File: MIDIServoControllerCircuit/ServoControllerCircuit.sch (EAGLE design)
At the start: 26 parts, among them Q1 20MHz, T1 2N3904, X1 SIGNAL-PWR-GND, X2 SIGNAL-PWR-GND

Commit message: Renamed directory to better reflect what files represent
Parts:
- D1: value 1N4198 -> 1N4148
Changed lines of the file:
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@@
 <part name="C1" library="resistor" deviceset="C-EU" device="050-025X075" value="22p"/>
 <part name="C2" library="resistor" deviceset="C-EU" device="050-025X075" value="22p"/>
-<part name="D1" library="diode" deviceset="1N4148" device="DO35-10" value="1N4198"/>
+<part name="D1" library="diode" deviceset="1N4148" device="DO35-10" value="1N4148"/>
 <part name="Q1" library="special" deviceset="XTAL/S" device="" value="20MHz"/>
 <part name="C3" library="resistor" deviceset="C-EU" device="050-025X075" value="0.1u"/>

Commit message: Renamed PWM outputs to better match what they go to
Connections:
- net SERVO1 renamed EYEBROW
- net SERVO2 renamed LEFT_LIP_CORNER
- net SERVO3 renamed RIGHT_LIP_CORNER
- net SERVO4 renamed LOWER_JAR
- net SERVO5 renamed EYELIDS
- net SERVO6 renamed UNUSED
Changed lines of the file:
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@@
 <instance part="GND8" gate="1" x="78.74" y="76.2" rot="R270"/>
 <instance part="GND9" gate="1" x="124.46" y="27.94" rot="R270"/>
-<instance part="GND10" gate="1" x="111.76" y="99.06"/>
-<instance part="GND11" gate="1" x="111.76" y="81.28"/>
-<instance part="GND13" gate="1" x="154.94" y="53.34"/>
-<instance part="GND14" gate="1" x="154.94" y="35.56"/>
+<instance part="GND10" gate="1" x="106.68" y="99.06"/>
+<instance part="GND11" gate="1" x="106.68" y="81.28"/>
+<instance part="GND13" gate="1" x="149.86" y="53.34"/>
+<instance part="GND14" gate="1" x="149.86" y="35.56"/>
 <instance part="MIDI_PIN-4" gate="1" x="25.4" y="81.28" smashed="yes" rot="R180">
 <attribute name="NAME" x="36.703" y="84.5058" size="1.778" layer="95" rot="R180"/>
@@
 <segment>
 <pinref part="PIC16F628A" gate="G$1" pin="7"/>
-<wire x1="55.88" y1="17.78" x2="43.18" y2="17.78" width="0.1524" layer="91"/>
-<wire x1="43.18" y1="17.78" x2="43.18" y2="2.54" width="0.1524" layer="91"/>
-<label x="43.18" y="2.54" size="1.778" layer="95" rot="R180" xref="yes"/>
+<wire x1="55.88" y1="17.78" x2="50.8" y2="17.78" width="0.1524" layer="91"/>
+<wire x1="50.8" y1="17.78" x2="50.8" y2="2.54" width="0.1524" layer="91"/>
+<label x="50.8" y="2.54" size="1.778" layer="95" rot="R180" xref="yes"/>
 </segment>
 </net>
@@
 <segment>
 <pinref part="X2" gate="-3" pin="S"/>
-<wire x1="114.3" y1="104.14" x2="111.76" y2="104.14" width="0.1524" layer="91"/>
-<wire x1="111.76" y1="104.14" x2="111.76" y2="101.6" width="0.1524" layer="91"/>
+<wire x1="114.3" y1="104.14" x2="106.68" y2="104.14" width="0.1524" layer="91"/>
+<wire x1="106.68" y1="104.14" x2="106.68" y2="101.6" width="0.1524" layer="91"/>
 <pinref part="GND10" gate="1" pin="GND"/>
 </segment>
 <segment>
 <pinref part="X2" gate="-6" pin="S"/>
-<wire x1="114.3" y1="86.36" x2="111.76" y2="86.36" width="0.1524" layer="91"/>
-<wire x1="111.76" y1="86.36" x2="111.76" y2="83.82" width="0.1524" layer="91"/>
+<wire x1="114.3" y1="86.36" x2="106.68" y2="86.36" width="0.1524" layer="91"/>
+<wire x1="106.68" y1="86.36" x2="106.68" y2="83.82" width="0.1524" layer="91"/>
 <pinref part="GND11" gate="1" pin="GND"/>
 </segment>
 <segment>
 <pinref part="X1" gate="-3" pin="S"/>
-<wire x1="157.48" y1="58.42" x2="154.94" y2="58.42" width="0.1524" layer="91"/>
-<wire x1="154.94" y1="58.42" x2="154.94" y2="55.88" width="0.1524" layer="91"/>
+<wire x1="157.48" y1="58.42" x2="149.86" y2="58.42" width="0.1524" layer="91"/>
+<wire x1="149.86" y1="58.42" x2="149.86" y2="55.88" width="0.1524" layer="91"/>
 <pinref part="GND13" gate="1" pin="GND"/>
 </segment>
 <segment>
 <pinref part="X1" gate="-6" pin="S"/>
-<wire x1="157.48" y1="40.64" x2="154.94" y2="40.64" width="0.1524" layer="91"/>
-<wire x1="154.94" y1="40.64" x2="154.94" y2="38.1" width="0.1524" layer="91"/>
+<wire x1="157.48" y1="40.64" x2="149.86" y2="40.64" width="0.1524" layer="91"/>
+<wire x1="149.86" y1="40.64" x2="149.86" y2="38.1" width="0.1524" layer="91"/>
 <pinref part="GND14" gate="1" pin="GND"/>
 </segment>
@@
 </segment>
 </net>
-<net name="SERVO3" class="0">
+<net name="RIGHT_LIP_CORNER" class="0">
 <segment>
 <pinref part="PIC16F628A" gate="G$1" pin="1"/>
@@
 <pinref part="X2" gate="-7" pin="S"/>
 <wire x1="114.3" y1="73.66" x2="111.76" y2="73.66" width="0.1524" layer="91"/>
-<wire x1="111.76" y1="73.66" x2="111.76" y2="76.2" width="0.1524" layer="91"/>
-<label x="111.76" y="76.2" size="1.778" layer="95" rot="R180" xref="yes"/>
-</segment>
-</net>
-<net name="SERVO1" class="0">
+<wire x1="111.76" y1="73.66" x2="111.76" y2="78.74" width="0.1524" layer="91"/>
+<label x="111.76" y="78.74" size="1.778" layer="95" xref="yes"/>
+</segment>
+</net>
+<net name="EYEBROW" class="0">
 <segment>
 <pinref part="PIC16F628A" gate="G$1" pin="17"/>
@@
 <pinref part="X2" gate="-1" pin="S"/>
 <wire x1="114.3" y1="109.22" x2="111.76" y2="109.22" width="0.1524" layer="91"/>
-<wire x1="111.76" y1="114.3" x2="111.76" y2="109.22" width="0.1524" layer="91"/>
-<label x="111.76" y="114.3" size="1.778" layer="95" rot="R180" xref="yes"/>
-</segment>
-</net>
-<net name="SERVO2" class="0">
+<wire x1="111.76" y1="116.84" x2="111.76" y2="109.22" width="0.1524" layer="91"/>
+<label x="111.76" y="116.84" size="1.778" layer="95" xref="yes"/>
+</segment>
+</net>
+<net name="LEFT_LIP_CORNER" class="0">
 <segment>
 <pinref part="PIC16F628A" gate="G$1" pin="18"/>
@@
 <pinref part="X2" gate="-4" pin="S"/>
 <wire x1="114.3" y1="91.44" x2="111.76" y2="91.44" width="0.1524" layer="91"/>
-<wire x1="111.76" y1="91.44" x2="111.76" y2="93.98" width="0.1524" layer="91"/>
-<label x="111.76" y="93.98" size="1.778" layer="95" rot="R180" xref="yes"/>
-</segment>
-</net>
-<net name="SERVO4" class="0">
+<wire x1="111.76" y1="91.44" x2="111.76" y2="96.52" width="0.1524" layer="91"/>
+<label x="111.76" y="96.52" size="1.778" layer="95" xref="yes"/>
+</segment>
+</net>
+<net name="LOWER_JAR" class="0">
 <segment>
 <pinref part="PIC16F628A" gate="G$1" pin="2"/>
@@
 <pinref part="X1" gate="-1" pin="S"/>
 <wire x1="157.48" y1="63.5" x2="154.94" y2="63.5" width="0.1524" layer="91"/>
-<wire x1="154.94" y1="63.5" x2="154.94" y2="66.04" width="0.1524" layer="91"/>
-<label x="154.94" y="66.04" size="1.778" layer="95" rot="R180" xref="yes"/>
-</segment>
-</net>
-<net name="SERVO5" class="0">
+<wire x1="154.94" y1="63.5" x2="154.94" y2="71.12" width="0.1524" layer="91"/>
+<label x="154.94" y="71.12" size="1.778" layer="95" xref="yes"/>
+</segment>
+</net>
+<net name="EYELIDS" class="0">
 <segment>
 <pinref part="PIC16F628A" gate="G$1" pin="6"/>
-<wire x1="55.88" y1="20.32" x2="38.1" y2="20.32" width="0.1524" layer="91"/>
-<wire x1="38.1" y1="20.32" x2="38.1" y2="7.62" width="0.1524" layer="91"/>
-<label x="38.1" y="7.62" size="1.778" layer="95" rot="R180" xref="yes"/>
+<wire x1="55.88" y1="20.32" x2="45.72" y2="20.32" width="0.1524" layer="91"/>
+<wire x1="45.72" y1="20.32" x2="45.72" y2="7.62" width="0.1524" layer="91"/>
+<label x="45.72" y="7.62" size="1.778" layer="95" rot="R180" xref="yes"/>
 </segment>
 <segment>
 <pinref part="X1" gate="-4" pin="S"/>
 <wire x1="157.48" y1="45.72" x2="154.94" y2="45.72" width="0.1524" layer="91"/>
-<wire x1="154.94" y1="45.72" x2="154.94" y2="48.26" width="0.1524" layer="91"/>
-<label x="154.94" y="48.26" size="1.778" layer="95" rot="R180" xref="yes"/>
-</segment>
-</net>
-<net name="SERVO6" class="0">
+<wire x1="154.94" y1="45.72" x2="154.94" y2="50.8" width="0.1524" layer="91"/>
+<label x="154.94" y="50.8" size="1.778" layer="95" xref="yes"/>
+</segment>
+</net>
+<net name="UNUSED" class="0">
 <segment>
 <pinref part="PIC16F628A" gate="G$1" pin="9"/>
 <wire x1="55.88" y1="12.7" x2="53.34" y2="12.7" width="0.1524" layer="91"/>
-<wire x1="53.34" y1="12.7" x2="53.34" y2="2.54" width="0.1524" layer="91"/>
-<label x="53.34" y="2.54" size="1.778" layer="95" xref="yes"/>
+<wire x1="53.34" y1="12.7" x2="53.34" y2="0" width="0.1524" layer="91"/>
+<label x="53.34" y="0" size="1.778" layer="95" xref="yes"/>
 </segment>
 <segment>
 <pinref part="X1" gate="-7" pin="S"/>
 <wire x1="157.48" y1="27.94" x2="154.94" y2="27.94" width="0.1524" layer="91"/>
-<wire x1="154.94" y1="27.94" x2="154.94" y2="30.48" width="0.1524" layer="91"/>
-<label x="154.94" y="30.48" size="1.778" layer="95" rot="R180" xref="yes"/>
-</segment>
-</net>
+<wire x1="154.94" y1="27.94" x2="154.94" y2="33.02" width="0.1524" layer="91"/>
+<label x="154.94" y="33.02" size="1.778" layer="95" xref="yes"/>
+</segment>
+</net>

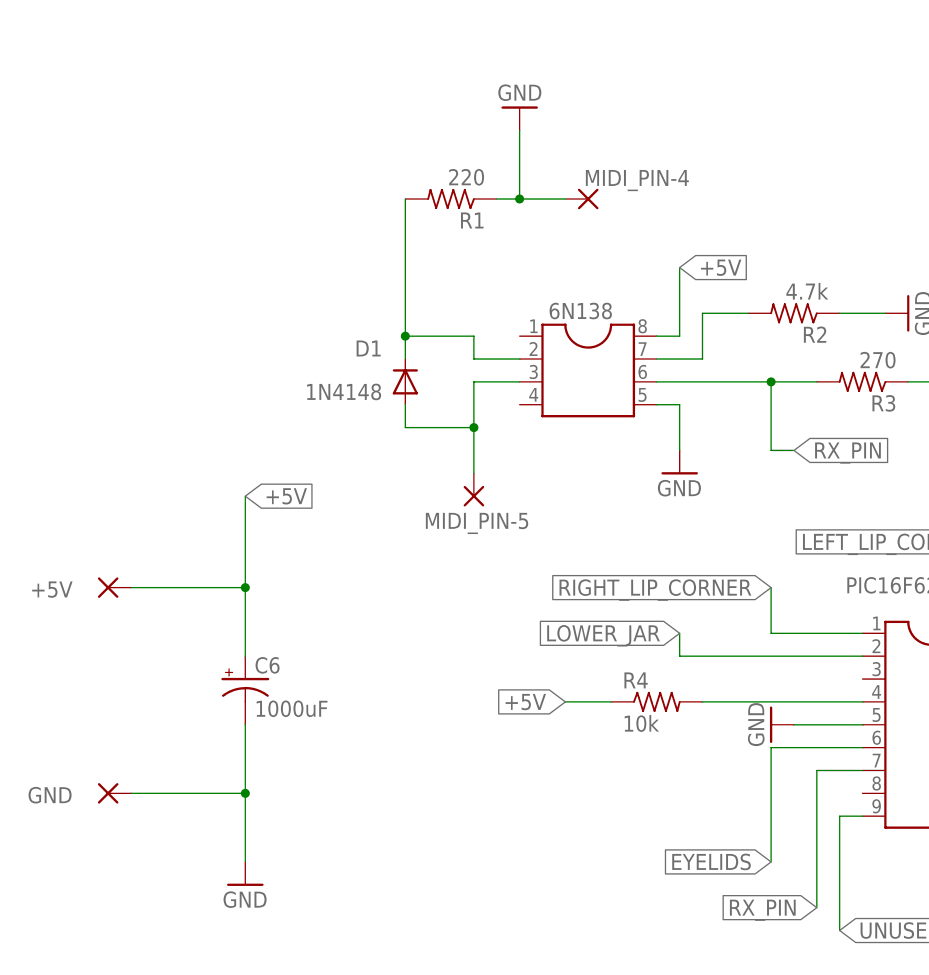
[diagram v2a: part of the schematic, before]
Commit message: Added Double Through Hole Pad and Holes to board
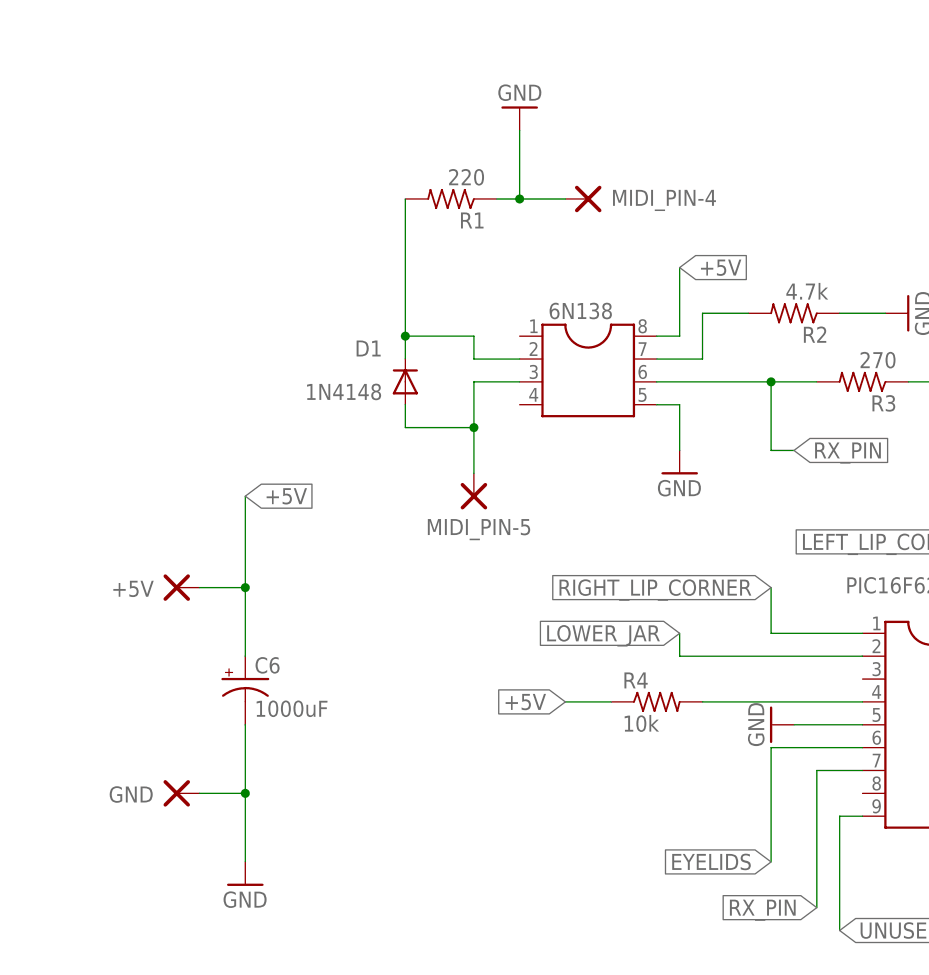
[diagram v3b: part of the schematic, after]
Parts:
- +5V, GND, MIDI_PIN-4, MIDI_PIN-5: value (none) -> DOUBLE_THROUGH_HOLE_PAD; device wirepad:2,15/1,0 -> DOUBLE_THROUGH_HOLE_PAD:DOUBLE_THROUGH_HOLE_PAD
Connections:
- net +5V: now also +5V.P$1; no longer +5V.P
- net GND: now also GND.P$1, MIDI_PIN-4.P$1; no longer GND.P, MIDI_PIN-4.P
- net MIDI_PIN-5: now also MIDI_PIN-5.P$1; no longer MIDI_PIN-5.P

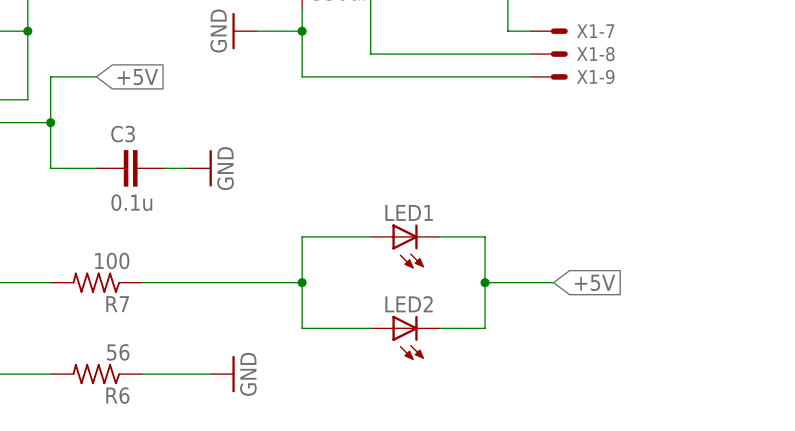
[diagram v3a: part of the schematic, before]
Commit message: Fixed LED directionality
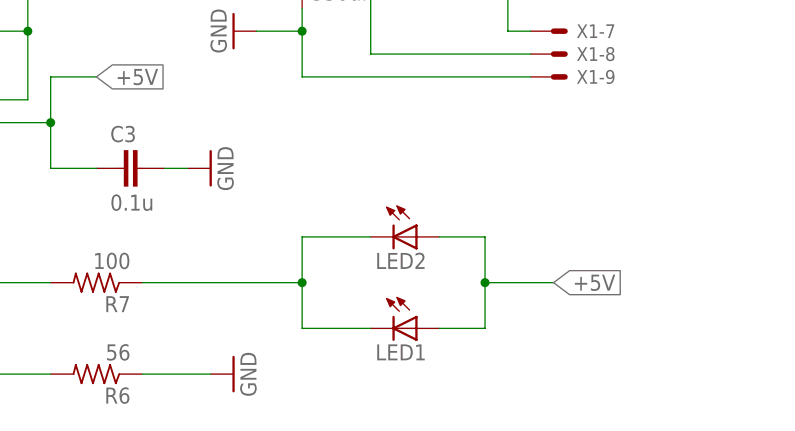
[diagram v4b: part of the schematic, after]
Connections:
- net +5V: now also LED1.A, LED2.A; no longer LED1.C, LED2.C
- net N$10: now also LED1.C, LED2.C; no longer LED1.A, LED2.A
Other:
- moved on the sheet: LED1, LED2
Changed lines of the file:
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@@
 <part name="R7" library="resistor" library_urn="urn:adsk.eagle:library:348" deviceset="R-US_" device="0207/12" package3d_urn="urn:adsk.eagle:package:25938/1" value="100"/>
 <part name="GND15" library="supply1" library_urn="urn:adsk.eagle:library:371" deviceset="GND" device=""/>
-<part name="LED1" library="led" library_urn="urn:adsk.eagle:library:259" deviceset="LED" device="5MM" package3d_urn="urn:adsk.eagle:package:15799/2"/>
-<part name="LED2" library="led" library_urn="urn:adsk.eagle:library:259" deviceset="LED" device="5MM" package3d_urn="urn:adsk.eagle:package:15799/2"/>
 <part name="T1" library="transistor" library_urn="urn:adsk.eagle:library:402" deviceset="2N3904" device="" package3d_urn="urn:adsk.eagle:package:29893/2"/>
 <part name="C6" library="resistor" library_urn="urn:adsk.eagle:library:348" deviceset="CPOL-US" device="E5-10.5" package3d_urn="urn:adsk.eagle:package:25854/1" value="1000uF"/>
@@
 <part name="MIDI_PIN-4" library="DOUBLE_THROUGH_HOLE_PAD" deviceset="DOUBLE_THROUGH_HOLE_PAD" device=""/>
 <part name="MIDI_PIN-5" library="DOUBLE_THROUGH_HOLE_PAD" deviceset="DOUBLE_THROUGH_HOLE_PAD" device=""/>
+<part name="LED2" library="led" library_urn="urn:adsk.eagle:library:259" deviceset="LED" device="5MM" package3d_urn="urn:adsk.eagle:package:15799/2"/>
+<part name="LED1" library="led" library_urn="urn:adsk.eagle:library:259" deviceset="LED" device="5MM" package3d_urn="urn:adsk.eagle:package:15799/2"/>
 </parts>
 <sheets>
@@
 <instance part="R7" gate="G$1" x="109.22" y="0" rot="R180"/>
 <instance part="GND15" gate="1" x="-12.7" y="5.08"/>
-<instance part="LED1" gate="G$1" x="142.24" y="5.08" rot="R90"/>
-<instance part="LED2" gate="G$1" x="142.24" y="-5.08" rot="R90"/>
 <instance part="T1" gate="G1" x="93.98" y="-5.08" smashed="yes">
 <attribute name="NAME" x="86.36" y="-10.16" size="1.778" layer="95"/>
@@
 <attribute name="NAME" x="7.366" y="43.942" size="1.778" layer="95"/>
 </instance>
+<instance part="LED2" gate="G$1" x="144.78" y="5.08" rot="R270"/>
+<instance part="LED1" gate="G$1" x="144.78" y="-5.08" rot="R270"/>
 </instances>
 <busses>
@@
 <wire x1="152.4" y1="0" x2="160.02" y2="0" width="0.1524" layer="91"/>
 <junction x="152.4" y="0"/>
-<pinref part="LED1" gate="G$1" pin="C"/>
-<pinref part="LED2" gate="G$1" pin="C"/>
 <label x="160.02" y="0" size="1.778" layer="95" xref="yes"/>
+<pinref part="LED2" gate="G$1" pin="A"/>
+<pinref part="LED1" gate="G$1" pin="A"/>
 </segment>
 </net>
@@
 <wire x1="132.08" y1="0" x2="132.08" y2="5.08" width="0.1524" layer="91"/>
 <wire x1="132.08" y1="5.08" x2="139.7" y2="5.08" width="0.1524" layer="91"/>
-<pinref part="LED1" gate="G$1" pin="A"/>
-<pinref part="LED2" gate="G$1" pin="A"/>
-</segment>
-</net>
+<pinref part="LED2" gate="G$1" pin="C"/>
+<pinref part="LED1" gate="G$1" pin="C"/>
+</segment>
+</net>

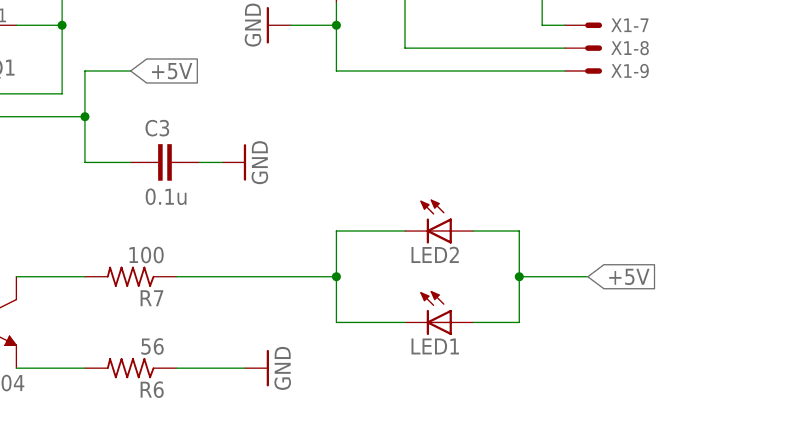
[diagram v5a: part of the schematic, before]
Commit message: Added Remote LED component and updated board layout
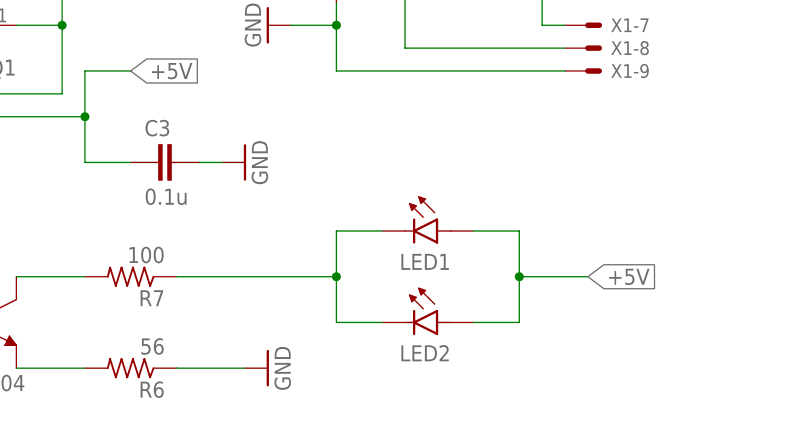
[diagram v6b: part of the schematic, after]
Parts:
- LED1, LED2: value (none) -> REMOTE_LED; device led:LED5MM -> REMOTE_LED:REMOTE_LED
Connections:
- net +5V: now also LED1.P$1, LED2.P$1; no longer LED1.A, LED2.A
- net N$10: now also LED1.P$2, LED2.P$2; no longer LED1.C, LED2.C
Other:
- moved on the sheet: LED1, LED2
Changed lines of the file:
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@@
 <part name="MIDI_PIN-4" library="DOUBLE_THROUGH_HOLE_PAD" deviceset="DOUBLE_THROUGH_HOLE_PAD" device=""/>
 <part name="MIDI_PIN-5" library="DOUBLE_THROUGH_HOLE_PAD" deviceset="DOUBLE_THROUGH_HOLE_PAD" device=""/>
-<part name="LED2" library="led" library_urn="urn:adsk.eagle:library:259" deviceset="LED" device="5MM" package3d_urn="urn:adsk.eagle:package:15799/2"/>
-<part name="LED1" library="led" library_urn="urn:adsk.eagle:library:259" deviceset="LED" device="5MM" package3d_urn="urn:adsk.eagle:package:15799/2"/>
+<part name="LED1" library="REMOTE_LED" deviceset="REMOTE_LED" device=""/>
+<part name="LED2" library="REMOTE_LED" deviceset="REMOTE_LED" device=""/>
 </parts>
 <sheets>
@@
 <attribute name="NAME" x="7.366" y="43.942" size="1.778" layer="95"/>
 </instance>
-<instance part="LED2" gate="G$1" x="144.78" y="5.08" rot="R270"/>
-<instance part="LED1" gate="G$1" x="144.78" y="-5.08" rot="R270"/>
+<instance part="LED1" gate="G$1" x="142.24" y="5.08" rot="R180"/>
+<instance part="LED2" gate="G$1" x="142.24" y="-5.08" rot="R180"/>
 </instances>
 <busses>
@@
 <junction x="152.4" y="0"/>
 <label x="160.02" y="0" size="1.778" layer="95" xref="yes"/>
-<pinref part="LED2" gate="G$1" pin="A"/>
-<pinref part="LED1" gate="G$1" pin="A"/>
+<pinref part="LED1" gate="G$1" pin="P$1"/>
+<pinref part="LED2" gate="G$1" pin="P$1"/>
 </segment>
 </net>
@@
 <junction x="132.08" y="0"/>
 <wire x1="132.08" y1="0" x2="132.08" y2="-5.08" width="0.1524" layer="91"/>
-<wire x1="132.08" y1="-5.08" x2="139.7" y2="-5.08" width="0.1524" layer="91"/>
 <wire x1="132.08" y1="0" x2="132.08" y2="5.08" width="0.1524" layer="91"/>
-<wire x1="132.08" y1="5.08" x2="139.7" y2="5.08" width="0.1524" layer="91"/>
-<pinref part="LED2" gate="G$1" pin="C"/>
-<pinref part="LED1" gate="G$1" pin="C"/>
-</segment>
-</net>
+<pinref part="LED1" gate="G$1" pin="P$2"/>
+<wire x1="132.08" y1="5.08" x2="137.16" y2="5.08" width="0.1524" layer="91"/>
+<pinref part="LED2" gate="G$1" pin="P$2"/>
+<wire x1="132.08" y1="-5.08" x2="137.16" y2="-5.08" width="0.1524" layer="91"/>
+</segment>
+</net>
